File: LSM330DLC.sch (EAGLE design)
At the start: 4 parts

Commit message: porzadki w plikach
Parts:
- C1: value (none) -> 100n
- C2: value (none) -> 10n
- C3: value (none) -> 10u
- renumbered ACC+GYRO to LSM330DLC
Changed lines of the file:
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@@
 <?xml version="1.0" encoding="utf-8"?>
 <!DOCTYPE eagle SYSTEM "eagle.dtd">
-<eagle version="6.3">
+<eagle version="6.2">
 <drawing>
 <settings>
@@
 </classes>
 <parts>
-<part name="ACC+GYRO" library="sensors-akc_zyr" deviceset="LSM330DLC" device=""/>
-<part name="C1" library="resistor" deviceset="C-EU" device="C0805"/>
-<part name="C2" library="resistor" deviceset="C-EU" device="C0805"/>
+<part name="LSM330DLC" library="sensors-akc_zyr" deviceset="LSM330DLC" device=""/>
+<part name="C1" library="resistor" deviceset="C-EU" device="C0805" value="100n"/>
+<part name="C2" library="resistor" deviceset="C-EU" device="C0805" value="10n"/>
 <part name="GND1" library="supply1" deviceset="GND" device=""/>
 <part name="GND2" library="supply1" deviceset="GND" device=""/>
-<part name="C3" library="rcl" deviceset="CPOL-EU" device="SMCA"/>
+<part name="C3" library="rcl" deviceset="CPOL-EU" device="SMCA" value="10u"/>
 <part name="SUPPLY1" library="SparkFun-Aesthetics" deviceset="3.3V" device=""/>
 <part name="SUPPLY2" library="SparkFun-Aesthetics" deviceset="3.3V" device=""/>
@@
 </plain>
 <instances>
-<instance part="ACC+GYRO" gate="G$1" x="43.18" y="116.84"/>
+<instance part="LSM330DLC" gate="G$1" x="43.18" y="116.84"/>
 <instance part="C1" gate="G$1" x="22.86" y="127" rot="R180"/>
 <instance part="C2" gate="G$1" x="33.02" y="142.24" rot="R270"/>
@@
 <net name="N$1" class="0">
 <segment>
-<pinref part="ACC+GYRO" gate="G$1" pin="CAP"/>
+<pinref part="LSM330DLC" gate="G$1" pin="CAP"/>
 <pinref part="C2" gate="G$1" pin="1"/>
 <wire x1="35.56" y1="142.24" x2="38.1" y2="142.24" width="0.1524" layer="91"/>
@@
 <net name="GND" class="0">
 <segment>
-<pinref part="ACC+GYRO" gate="G$1" pin="VSS"/>
+<pinref part="LSM330DLC" gate="G$1" pin="VSS"/>
 <pinref part="GND2" gate="1" pin="GND"/>
 <pinref part="C3" gate="G$1" pin="-"/>
@@
 </segment>
 <segment>
-<pinref part="ACC+GYRO" gate="G$1" pin="SDO_A"/>
-<pinref part="ACC+GYRO" gate="G$1" pin="SDO_G"/>
+<pinref part="LSM330DLC" gate="G$1" pin="SDO_A"/>
+<pinref part="LSM330DLC" gate="G$1" pin="SDO_G"/>
 <wire x1="38.1" y1="157.48" x2="38.1" y2="162.56" width="0.1524" layer="91"/>
 <wire x1="38.1" y1="162.56" x2="22.86" y2="162.56" width="0.1524" layer="91"/>
@@
 </segment>
 <segment>
-<pinref part="ACC+GYRO" gate="G$1" pin="DEN_G"/>
+<pinref part="LSM330DLC" gate="G$1" pin="DEN_G"/>
 <pinref part="GND4" gate="1" pin="GND"/>
 <wire x1="81.28" y1="162.56" x2="91.44" y2="162.56" width="0.1524" layer="91"/>
@@
 <net name="3.3V" class="0">
 <segment>
-<pinref part="ACC+GYRO" gate="G$1" pin="VDD"/>
-<pinref part="ACC+GYRO" gate="G$1" pin="VDD_IO"/>
+<pinref part="LSM330DLC" gate="G$1" pin="VDD"/>
+<pinref part="LSM330DLC" gate="G$1" pin="VDD_IO"/>
 <wire x1="38.1" y1="127" x2="38.1" y2="132.08" width="0.1524" layer="91"/>
 <pinref part="C1" gate="G$1" pin="2"/>
@@
 </segment>
 <segment>
-<pinref part="ACC+GYRO" gate="G$1" pin="!CS_A"/>
-<pinref part="ACC+GYRO" gate="G$1" pin="!CS_G"/>
+<pinref part="LSM330DLC" gate="G$1" pin="!CS_A"/>
+<pinref part="LSM330DLC" gate="G$1" pin="!CS_G"/>
 <wire x1="38.1" y1="172.72" x2="38.1" y2="177.8" width="0.1524" layer="91"/>
 <wire x1="38.1" y1="177.8" x2="20.32" y2="177.8" width="0.1524" layer="91"/>
@@
 <net name="SCL" class="0">
 <segment>
-<pinref part="ACC+GYRO" gate="G$1" pin="SCL"/>
+<pinref part="LSM330DLC" gate="G$1" pin="SCL"/>
 <wire x1="38.1" y1="167.64" x2="30.48" y2="167.64" width="0.1524" layer="91"/>
 <label x="25.4" y="167.64" size="1.778" layer="95"/>
@@
 <net name="SDA" class="0">
 <segment>
-<pinref part="ACC+GYRO" gate="G$1" pin="SDA"/>
+<pinref part="LSM330DLC" gate="G$1" pin="SDA"/>
 <wire x1="38.1" y1="152.4" x2="30.48" y2="152.4" width="0.1524" layer="91"/>
 <label x="25.4" y="152.4" size="1.778" layer="95"/>
@@
 <net name="INT_ACC" class="0">
 <segment>
-<pinref part="ACC+GYRO" gate="G$1" pin="INT1_A"/>
+<pinref part="LSM330DLC" gate="G$1" pin="INT1_A"/>
 <wire x1="81.28" y1="172.72" x2="86.36" y2="172.72" width="0.1524" layer="91"/>
 <label x="86.36" y="172.72" size="1.778" layer="95"/>
@@
 <net name="INT_GYRO" class="0">
 <segment>
-<pinref part="ACC+GYRO" gate="G$1" pin="INT1_G"/>
+<pinref part="LSM330DLC" gate="G$1" pin="INT1_G"/>
 <wire x1="81.28" y1="152.4" x2="86.36" y2="152.4" width="0.1524" layer="91"/>
 <label x="86.36" y="152.4" size="1.778" layer="95"/>

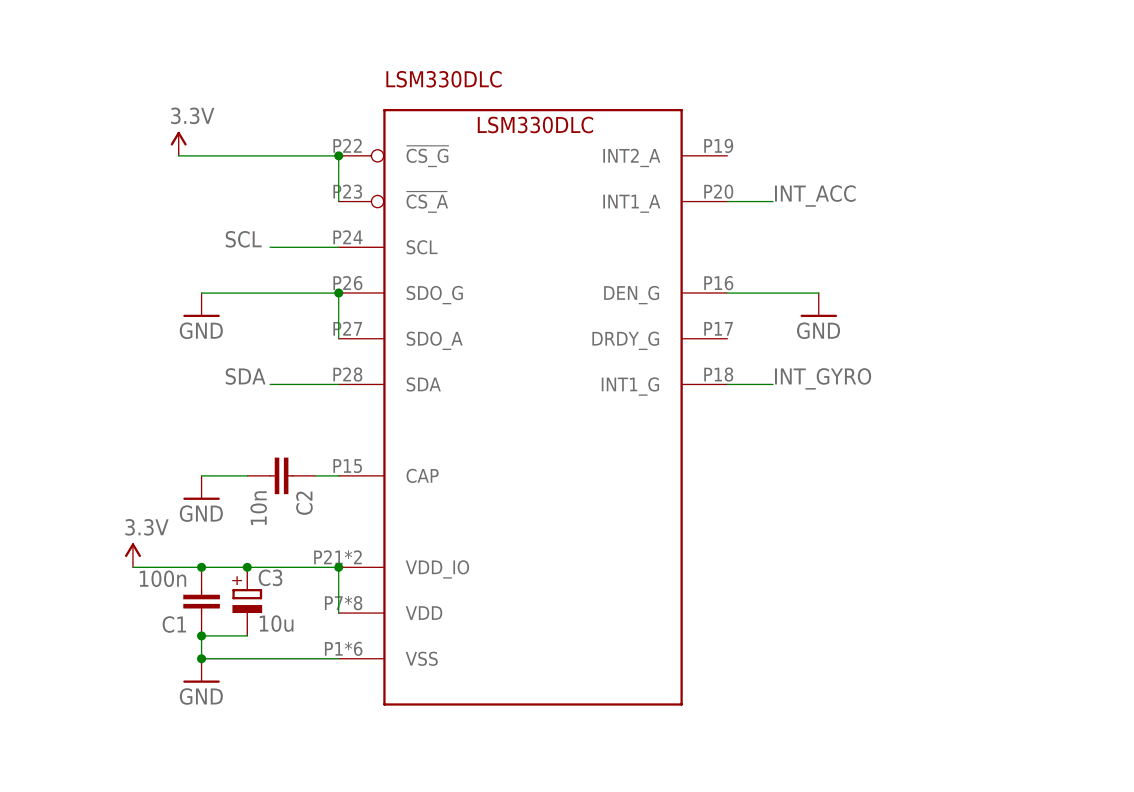
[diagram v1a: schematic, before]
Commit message: dodane obwodki z nazwami dla poszczegolnych elementow
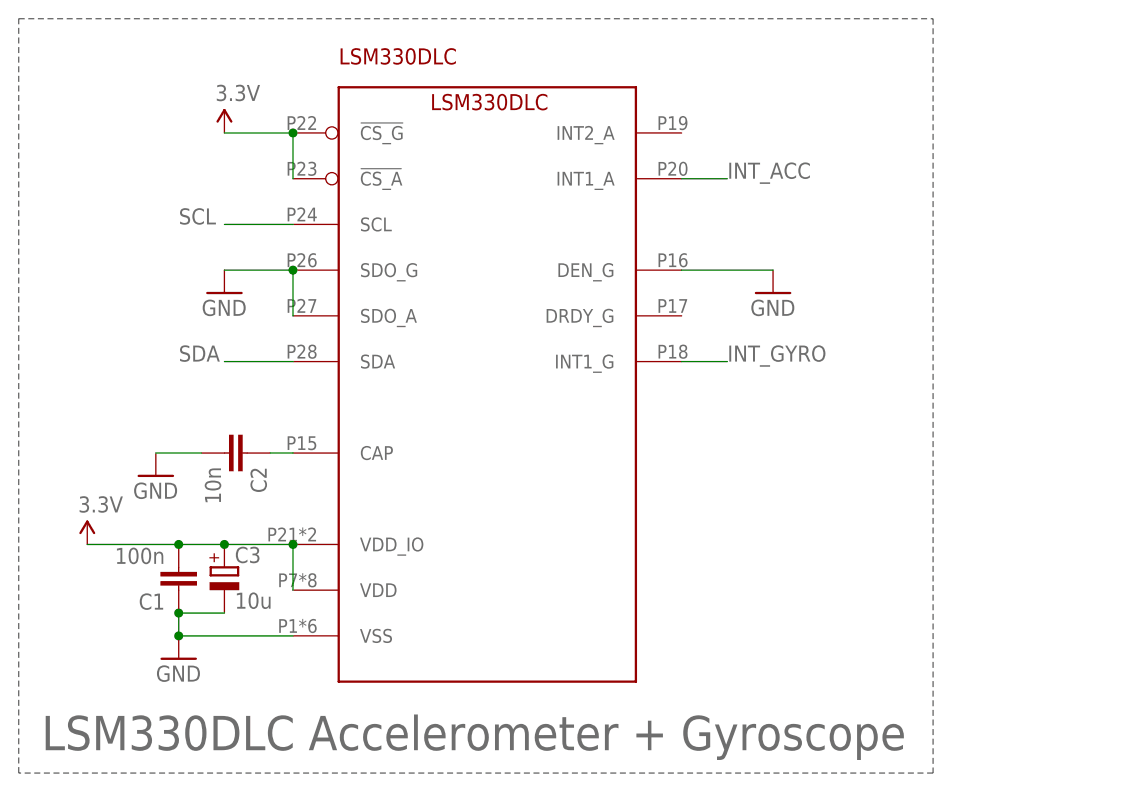
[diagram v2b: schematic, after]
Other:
- note added: "LSM330DLC Accelerometer + Gyroscope"
- moved on the sheet: C1, C2, C3, LSM330DLC
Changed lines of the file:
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@@
 <sheet>
 <plain>
+<wire x1="2.54" y1="193.04" x2="104.14" y2="193.04" width="0.1524" layer="95" style="shortdash"/>
+<wire x1="104.14" y1="193.04" x2="104.14" y2="109.22" width="0.1524" layer="95" style="shortdash"/>
+<wire x1="104.14" y1="109.22" x2="2.54" y2="109.22" width="0.1524" layer="95" style="shortdash"/>
+<wire x1="2.54" y1="109.22" x2="2.54" y2="193.04" width="0.1524" layer="95" style="shortdash"/>
+<text x="5.08" y="111.76" size="3.81" layer="95">LSM330DLC Accelerometer + Gyroscope</text>
 </plain>
 <instances>
-<instance part="LSM330DLC" gate="G$1" x="43.18" y="116.84"/>
-<instance part="C1" gate="G$1" x="22.86" y="127" rot="R180"/>
-<instance part="C2" gate="G$1" x="33.02" y="142.24" rot="R270"/>
-<instance part="GND1" gate="1" x="22.86" y="139.7"/>
-<instance part="GND2" gate="1" x="22.86" y="119.38"/>
-<instance part="C3" gate="G$1" x="27.94" y="129.54"/>
-<instance part="SUPPLY1" gate="G$1" x="15.24" y="132.08"/>
-<instance part="SUPPLY2" gate="G$1" x="20.32" y="177.8"/>
-<instance part="GND3" gate="1" x="22.86" y="160.02"/>
-<instance part="GND4" gate="1" x="91.44" y="160.02"/>
+<instance part="LSM330DLC" gate="G$1" x="38.1" y="119.38"/>
+<instance part="C1" gate="G$1" x="20.32" y="129.54" rot="R180"/>
+<instance part="C2" gate="G$1" x="27.94" y="144.78" rot="R270"/>
+<instance part="GND1" gate="1" x="17.78" y="142.24"/>
+<instance part="GND2" gate="1" x="20.32" y="121.92"/>
+<instance part="C3" gate="G$1" x="25.4" y="132.08"/>
+<instance part="SUPPLY1" gate="G$1" x="10.16" y="134.62"/>
+<instance part="SUPPLY2" gate="G$1" x="25.4" y="180.34"/>
+<instance part="GND3" gate="1" x="25.4" y="162.56"/>
+<instance part="GND4" gate="1" x="86.36" y="162.56"/>
 </instances>
 <busses>
@@
 <pinref part="LSM330DLC" gate="G$1" pin="CAP"/>
 <pinref part="C2" gate="G$1" pin="1"/>
-<wire x1="35.56" y1="142.24" x2="38.1" y2="142.24" width="0.1524" layer="91"/>
+<wire x1="30.48" y1="144.78" x2="33.02" y2="144.78" width="0.1524" layer="91"/>
 </segment>
 </net>
@@
 <pinref part="C3" gate="G$1" pin="-"/>
 <pinref part="C1" gate="G$1" pin="1"/>
-<wire x1="27.94" y1="124.46" x2="22.86" y2="124.46" width="0.1524" layer="91"/>
-<wire x1="22.86" y1="124.46" x2="22.86" y2="121.92" width="0.1524" layer="91"/>
-<junction x="22.86" y="124.46"/>
-<junction x="22.86" y="121.92"/>
-<wire x1="22.86" y1="121.92" x2="38.1" y2="121.92" width="0.1524" layer="91"/>
+<wire x1="25.4" y1="127" x2="20.32" y2="127" width="0.1524" layer="91"/>
+<wire x1="20.32" y1="127" x2="20.32" y2="124.46" width="0.1524" layer="91"/>
+<junction x="20.32" y="127"/>
+<junction x="20.32" y="124.46"/>
+<wire x1="20.32" y1="124.46" x2="33.02" y2="124.46" width="0.1524" layer="91"/>
 </segment>
 <segment>
 <pinref part="C2" gate="G$1" pin="2"/>
 <pinref part="GND1" gate="1" pin="GND"/>
-<wire x1="27.94" y1="142.24" x2="22.86" y2="142.24" width="0.1524" layer="91"/>
+<wire x1="22.86" y1="144.78" x2="17.78" y2="144.78" width="0.1524" layer="91"/>
 </segment>
 <segment>
 <pinref part="LSM330DLC" gate="G$1" pin="SDO_A"/>
 <pinref part="LSM330DLC" gate="G$1" pin="SDO_G"/>
-<wire x1="38.1" y1="157.48" x2="38.1" y2="162.56" width="0.1524" layer="91"/>
-<wire x1="38.1" y1="162.56" x2="22.86" y2="162.56" width="0.1524" layer="91"/>
+<wire x1="33.02" y1="160.02" x2="33.02" y2="165.1" width="0.1524" layer="91"/>
+<wire x1="33.02" y1="165.1" x2="25.4" y2="165.1" width="0.1524" layer="91"/>
 <pinref part="GND3" gate="1" pin="GND"/>
-<junction x="38.1" y="162.56"/>
+<junction x="33.02" y="165.1"/>
 </segment>
 <segment>
 <pinref part="LSM330DLC" gate="G$1" pin="DEN_G"/>
 <pinref part="GND4" gate="1" pin="GND"/>
-<wire x1="81.28" y1="162.56" x2="91.44" y2="162.56" width="0.1524" layer="91"/>
+<wire x1="76.2" y1="165.1" x2="86.36" y2="165.1" width="0.1524" layer="91"/>
 </segment>
 </net>
@@
 <pinref part="LSM330DLC" gate="G$1" pin="VDD"/>
 <pinref part="LSM330DLC" gate="G$1" pin="VDD_IO"/>
-<wire x1="38.1" y1="127" x2="38.1" y2="132.08" width="0.1524" layer="91"/>
+<wire x1="33.02" y1="129.54" x2="33.02" y2="134.62" width="0.1524" layer="91"/>
 <pinref part="C1" gate="G$1" pin="2"/>
-<wire x1="22.86" y1="132.08" x2="27.94" y2="132.08" width="0.1524" layer="91"/>
-<junction x="38.1" y="132.08"/>
+<wire x1="20.32" y1="134.62" x2="25.4" y2="134.62" width="0.1524" layer="91"/>
+<junction x="33.02" y="134.62"/>
 <pinref part="C3" gate="G$1" pin="+"/>
-<junction x="27.94" y="132.08"/>
-<wire x1="27.94" y1="132.08" x2="38.1" y2="132.08" width="0.1524" layer="91"/>
-<wire x1="22.86" y1="132.08" x2="15.24" y2="132.08" width="0.1524" layer="91"/>
+<junction x="25.4" y="134.62"/>
+<wire x1="25.4" y1="134.62" x2="33.02" y2="134.62" width="0.1524" layer="91"/>
+<wire x1="20.32" y1="134.62" x2="10.16" y2="134.62" width="0.1524" layer="91"/>
 <pinref part="SUPPLY1" gate="G$1" pin="3.3V"/>
-<junction x="22.86" y="132.08"/>
+<junction x="20.32" y="134.62"/>
 </segment>
 <segment>
 <pinref part="LSM330DLC" gate="G$1" pin="!CS_A"/>
 <pinref part="LSM330DLC" gate="G$1" pin="!CS_G"/>
-<wire x1="38.1" y1="172.72" x2="38.1" y2="177.8" width="0.1524" layer="91"/>
-<wire x1="38.1" y1="177.8" x2="20.32" y2="177.8" width="0.1524" layer="91"/>
+<wire x1="33.02" y1="175.26" x2="33.02" y2="180.34" width="0.1524" layer="91"/>
+<wire x1="33.02" y1="180.34" x2="25.4" y2="180.34" width="0.1524" layer="91"/>
 <pinref part="SUPPLY2" gate="G$1" pin="3.3V"/>
-<junction x="38.1" y="177.8"/>
+<junction x="33.02" y="180.34"/>
 </segment>
 </net>
@@
 <segment>
 <pinref part="LSM330DLC" gate="G$1" pin="SCL"/>
-<wire x1="38.1" y1="167.64" x2="30.48" y2="167.64" width="0.1524" layer="91"/>
-<label x="25.4" y="167.64" size="1.778" layer="95"/>
+<wire x1="33.02" y1="170.18" x2="25.4" y2="170.18" width="0.1524" layer="91"/>
+<label x="20.32" y="170.18" size="1.778" layer="95"/>
 </segment>
 </net>
@@
 <segment>
 <pinref part="LSM330DLC" gate="G$1" pin="SDA"/>
-<wire x1="38.1" y1="152.4" x2="30.48" y2="152.4" width="0.1524" layer="91"/>
-<label x="25.4" y="152.4" size="1.778" layer="95"/>
+<wire x1="33.02" y1="154.94" x2="25.4" y2="154.94" width="0.1524" layer="91"/>
+<label x="20.32" y="154.94" size="1.778" layer="95"/>
 </segment>
 </net>
@@
 <segment>
 <pinref part="LSM330DLC" gate="G$1" pin="INT1_A"/>
-<wire x1="81.28" y1="172.72" x2="86.36" y2="172.72" width="0.1524" layer="91"/>
-<label x="86.36" y="172.72" size="1.778" layer="95"/>
+<wire x1="76.2" y1="175.26" x2="81.28" y2="175.26" width="0.1524" layer="91"/>
+<label x="81.28" y="175.26" size="1.778" layer="95"/>
 </segment>
 </net>
@@
 <segment>
 <pinref part="LSM330DLC" gate="G$1" pin="INT1_G"/>
-<wire x1="81.28" y1="152.4" x2="86.36" y2="152.4" width="0.1524" layer="91"/>
-<label x="86.36" y="152.4" size="1.778" layer="95"/>
+<wire x1="76.2" y1="154.94" x2="81.28" y2="154.94" width="0.1524" layer="91"/>
+<label x="81.28" y="154.94" size="1.778" layer="95"/>
 </segment>
 </net>
